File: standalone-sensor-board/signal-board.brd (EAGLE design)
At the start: 26 x 93.5 mm, 32 parts, among them Q1 QRE1113, Q2 QRE1113, Q3 QRE1113, Q4 QRE1113, Q5 QRE1113, Q6 QRE1113, Q7 QRE1113, U1 CD4051BE

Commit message: rough layout
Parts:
- removed FFCIN, FFCOUT: 52806-1410, 52806-1410:528061410
- removed Q1, Q2, Q3, Q4, Q5, Q6, Q7: QRE1113, qre1113:DIP4_100AQ_ONS
- removed R1, R11, R13, R3, R5, R7, R9: 100, rcl:0207/10
- added J1, J3, J4: (no value), 686114148922:686114148922
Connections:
- removed net N$1: Q1.1, R1.2
- removed net N$11: Q6.1, R11.2
- removed net N$13: Q7.1, R13.2
- removed net N$2: FFCOUT.3, R1.1, R11.1, R13.1, R3.1, R5.1, R7.1, R9.1
- removed net N$3: Q2.1, R3.2
- removed net N$5: Q3.1, R5.2
- removed net N$7: Q4.1, R7.2
- net 3V: now also J3.13, J4.13; no longer FFCIN.13, FFCOUT.2
- net A: now also J3.11, J4.11; no longer FFCIN.11, FFCOUT.4
- net B: now also J3.10, J4.10; no longer FFCIN.10, FFCOUT.5
- net C: now also J3.9, J4.9; no longer FFCIN.9, FFCOUT.6
- net C0: now also J1.1; no longer Q1.3
- net C1: now also J1.2; no longer Q2.3
- net C2: now also J1.3; no longer Q3.3
- net C3: now also J1.9; no longer Q4.3
- net C4: now also J1.10; no longer Q5.3
- net C5: now also J1.11; no longer Q6.3
- net C6: now also J1.12; no longer Q7.3
- net DIN: now also J4.8; no longer FFCIN.8
- net DOUT: now also J3.8; no longer FFCOUT.7
- net GND: now also J1.14, J1.MP1, J1.MP2, J3.14, J3.MP1, J3.MP2, J4.14, J4.MP1, J4.MP2; no longer FFCOUT.1, Q1.2, Q1.4, Q2.2, Q2.4, Q3.2, Q3.4, Q4.2, Q4.4, Q5.2, Q5.4, Q6.2, Q6.4, Q7.2, Q7.4
- net S1: now also J3.7, J4.7; no longer FFCIN.7, FFCOUT.8
- net S2: now also J3.6, J4.6; no longer FFCIN.6, FFCOUT.9
- net S3: now also J3.5, J4.5; no longer FFCIN.5, FFCOUT.10
- net S4: now also J3.4, J4.4; no longer FFCIN.4, FFCOUT.11
- net S5: now also J3.3, J4.3; no longer FFCIN.3, FFCOUT.12
- net S6: now also J3.2, J4.2; no longer FFCIN.2, FFCOUT.13
- net S7: now also J3.1, J4.1; no longer FFCIN.1, FFCOUT.14
- net VCC: now also J1.13, J3.12, J4.12; no longer FFCIN.12
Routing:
- net S6: track 89.6 -> 0.00 mm, vias 2 -> 0
- net S4: track 88.9 -> 2.46 mm, vias 2 -> 0
- net S5: track 85.4 -> 3.87 mm, vias 2 -> 0
- net S2: track 85.8 -> 5.08 mm, vias 2 -> 0
- net B: track 79.3 -> 0.00 mm
- net S1: track 79.2 -> 3.02 mm, vias 2 -> 0
- net S3: track 78.6 -> 6.75 mm, vias 2 -> 0
- net C: track 68.1 -> 0.00 mm
- net C1: track 66.8 -> 0.00 mm, vias 3 -> 0
- net A: track 65.9 -> 0.00 mm
- net N$13: track 60.4 -> 0.00 mm
- net C0: track 50.8 -> 0.00 mm
- net N$11: track 49.1 -> 0.00 mm
- net C6: track 48.3 -> 0.00 mm
- net C5: track 29.0 -> 0.00 mm
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
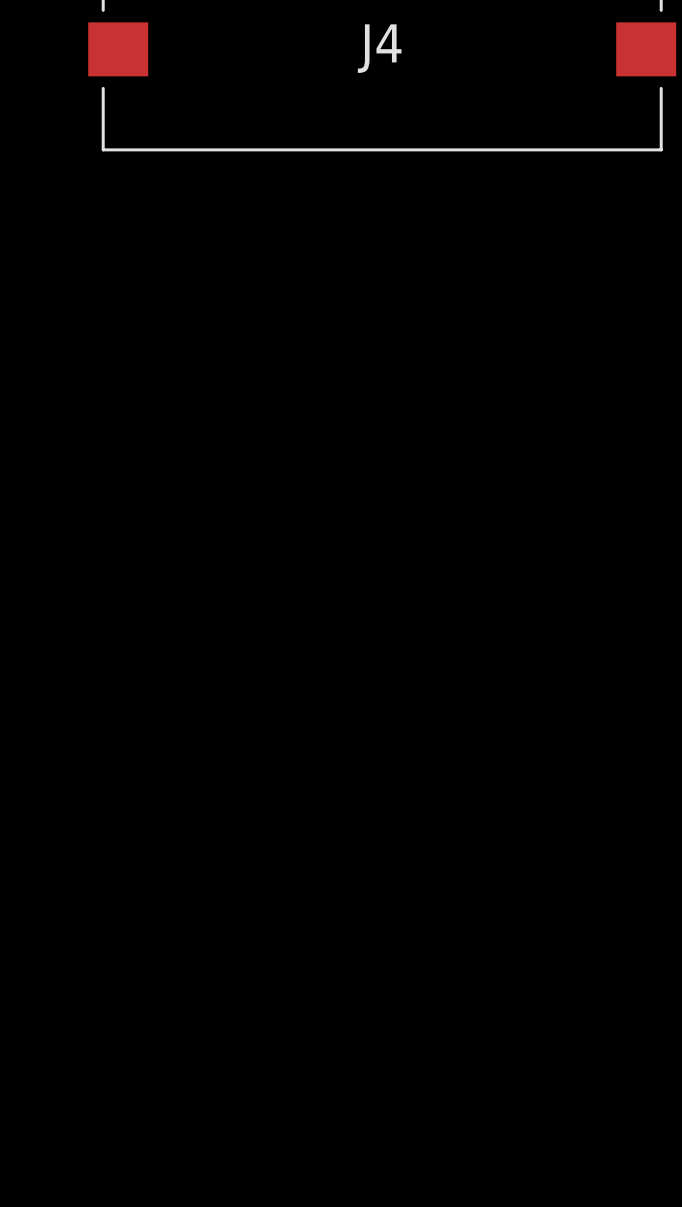
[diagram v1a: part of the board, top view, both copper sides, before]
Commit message: add divider resistors
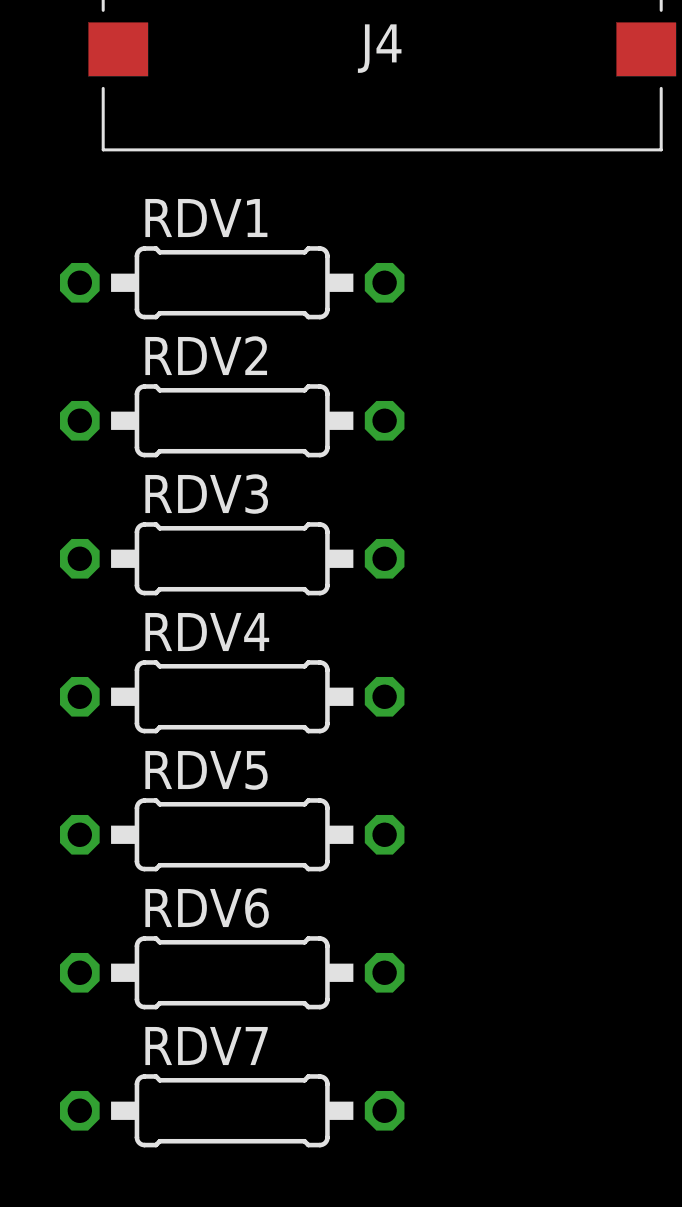
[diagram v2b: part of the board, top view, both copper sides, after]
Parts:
- added RDV1, RDV2, RDV3, RDV4, RDV5, RDV6, RDV7: 100k, rcl:0207/10
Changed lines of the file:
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@@
 <attribute name="VALUE" x="-31.76" y="-40.74" size="1.27" layer="27" align="center"/>
+</element>
+<element name="RDV1" library="rcl" library_urn="urn:adsk.eagle:library:334" package="0207/10" package3d_urn="urn:adsk.eagle:package:23491/2" value="100k" x="-36.76" y="-48.72" smashed="yes">
+<attribute name="NAME" x="-39.808" y="-47.196" size="1.27" layer="25" ratio="10"/>
+<attribute name="POPULARITY" value="81" x="-36.76" y="-48.72" size="1.778" layer="27" display="off"/>
+<attribute name="SPICEPREFIX" value="R" x="-36.76" y="-48.72" size="1.778" layer="27" display="off"/>
+<attribute name="VALUE" x="-39.0206" y="-49.355" size="1.27" layer="27" ratio="10"/>
+</element>
+<element name="RDV2" library="rcl" library_urn="urn:adsk.eagle:library:334" package="0207/10" package3d_urn="urn:adsk.eagle:package:23491/2" value="100k" x="-36.76" y="-53.32" smashed="yes">
+<attribute name="NAME" x="-39.808" y="-51.796" size="1.27" layer="25" ratio="10"/>
+<attribute name="POPULARITY" value="81" x="-36.76" y="-53.32" size="1.778" layer="27" display="off"/>
+<attribute name="SPICEPREFIX" value="R" x="-36.76" y="-53.32" size="1.778" layer="27" display="off"/>
+<attribute name="VALUE" x="-39.0206" y="-53.955" size="1.27" layer="27" ratio="10"/>
+</element>
+<element name="RDV3" library="rcl" library_urn="urn:adsk.eagle:library:334" package="0207/10" package3d_urn="urn:adsk.eagle:package:23491/2" value="100k" x="-36.76" y="-57.92" smashed="yes">
+<attribute name="NAME" x="-39.808" y="-56.396" size="1.27" layer="25" ratio="10"/>
+<attribute name="POPULARITY" value="81" x="-36.76" y="-57.92" size="1.778" layer="27" display="off"/>
+<attribute name="SPICEPREFIX" value="R" x="-36.76" y="-57.92" size="1.778" layer="27" display="off"/>
+<attribute name="VALUE" x="-39.0206" y="-58.555" size="1.27" layer="27" ratio="10"/>
+</element>
+<element name="RDV4" library="rcl" library_urn="urn:adsk.eagle:library:334" package="0207/10" package3d_urn="urn:adsk.eagle:package:23491/2" value="100k" x="-36.76" y="-62.52" smashed="yes">
+<attribute name="NAME" x="-39.808" y="-60.996" size="1.27" layer="25" ratio="10"/>
+<attribute name="POPULARITY" value="81" x="-36.76" y="-62.52" size="1.778" layer="27" display="off"/>
+<attribute name="SPICEPREFIX" value="R" x="-36.76" y="-62.52" size="1.778" layer="27" display="off"/>
+<attribute name="VALUE" x="-39.0206" y="-63.155" size="1.27" layer="27" ratio="10"/>
+</element>
+<element name="RDV5" library="rcl" library_urn="urn:adsk.eagle:library:334" package="0207/10" package3d_urn="urn:adsk.eagle:package:23491/2" value="100k" x="-36.76" y="-67.12" smashed="yes">
+<attribute name="NAME" x="-39.808" y="-65.596" size="1.27" layer="25" ratio="10"/>
+<attribute name="POPULARITY" value="81" x="-36.76" y="-67.12" size="1.778" layer="27" display="off"/>
+<attribute name="SPICEPREFIX" value="R" x="-36.76" y="-67.12" size="1.778" layer="27" display="off"/>
+<attribute name="VALUE" x="-39.0206" y="-67.755" size="1.27" layer="27" ratio="10"/>
+</element>
+<element name="RDV6" library="rcl" library_urn="urn:adsk.eagle:library:334" package="0207/10" package3d_urn="urn:adsk.eagle:package:23491/2" value="100k" x="-36.76" y="-71.72" smashed="yes">
+<attribute name="NAME" x="-39.808" y="-70.196" size="1.27" layer="25" ratio="10"/>
+<attribute name="POPULARITY" value="81" x="-36.76" y="-71.72" size="1.778" layer="27" display="off"/>
+<attribute name="SPICEPREFIX" value="R" x="-36.76" y="-71.72" size="1.778" layer="27" display="off"/>
+<attribute name="VALUE" x="-39.0206" y="-72.355" size="1.27" layer="27" ratio="10"/>
+</element>
+<element name="RDV7" library="rcl" library_urn="urn:adsk.eagle:library:334" package="0207/10" package3d_urn="urn:adsk.eagle:package:23491/2" value="100k" x="-36.76" y="-76.32" smashed="yes">
+<attribute name="NAME" x="-39.808" y="-74.796" size="1.27" layer="25" ratio="10"/>
+<attribute name="POPULARITY" value="81" x="-36.76" y="-76.32" size="1.778" layer="27" display="off"/>
+<attribute name="SPICEPREFIX" value="R" x="-36.76" y="-76.32" size="1.778" layer="27" display="off"/>
+<attribute name="VALUE" x="-39.0206" y="-76.955" size="1.27" layer="27" ratio="10"/>
 </element>
 </elements>

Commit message: set rdvs
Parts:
- removed D1, D2, D3, D4, D5, D6, D7: 1655, 1655:LED_1655
- removed RDV: 100k, rcl:0207/10
- added LED1, LED2, LED3, LED4, LED5, LED6, LED7: WS2812B3535, adafruit:LED3535
- J1: value (none) -> sensors
- J3: value (none) -> to_next_board
- J4: value (none) -> to_controller
- moved J3 128.1 mm to (11.0, 88.7), turned to 180 degrees
- moved RDV7 124.7 mm to (15.1, 37.1)
- moved RDV6 122.9 mm to (15.1, 39.7)
- moved RDV5 121.1 mm to (15.1, 42.3)
- moved RDV4 119.3 mm to (15.1, 44.9)
- moved RDV3 117.5 mm to (15.1, 47.5)
- moved RDV2 115.7 mm to (15.1, 50.1)
- moved RDV1 113.9 mm to (15.1, 52.7)
- moved J1 71.6 mm to (5.00, 47.8), turned to 270 degrees
- moved J4 62.6 mm to (11.1, 4.44)
- moved U1 47.0 mm to (15.4, 14.9), turned to 180 degrees
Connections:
- removed net N$15: D6.4, D7.2
- removed net N$16: D1.4, D2.2
- removed net N$17: D2.4, D3.2
- removed net N$18: D3.4, D4.2
- removed net N$19: D4.4, D5.2
- removed net N$20: D5.4, D6.2
- new net N$1: LED1.3, LED2.1
- new net N$2: LED2.3, LED3.1
- new net N$3: LED3.3, LED4.1
- new net N$4: LED4.3, LED5.1
- new net N$5: LED5.3, LED6.1
- new net N$6: LED6.3, LED7.1
- net 3V: now also LED1.2, LED2.2, LED3.2, LED4.2, LED5.2, LED6.2, LED7.2; no longer D1.3, D2.3, D3.3, D4.3, D5.3, D6.3, D7.3
- net C0: now also RDV1.2
- net C1: now also RDV2.2
- net C2: now also RDV3.2
- net C3: now also RDV4.2
- net C4: now also RDV5.2
- net C5: now also RDV6.2
- net C6: now also RDV7.2
- net DIN: now also LED1.1; no longer D1.2
- net DOUT: now also LED7.3; no longer D7.4
- net GND: now also LED1.4, LED2.4, LED3.4, LED4.4, LED5.4, LED6.4, LED7.4; no longer D1.1, D2.1, D3.1, D4.1, D5.1, D6.1, D7.1
- net SIG: no longer RDV.1
- net VCC: now also RDV1.1, RDV2.1, RDV3.1, RDV4.1, RDV5.1, RDV6.1, RDV7.1; no longer RDV.2
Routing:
- net 3V: track 116.5 -> 0.00 mm
- net GND: track 106.6 -> 0.00 mm, vias 7 -> 0
- net S7: track 79.6 -> 0.00 mm, vias 1 -> 0
- net SIG: track 36.0 -> 0.00 mm
- net VCC: track 19.5 -> 0.00 mm
- net DOUT: track 15.2 -> 0.00 mm, vias 1 -> 0
- net DIN: track 12.9 -> 0.00 mm, vias 1 -> 0
- net N$17: track 12.0 -> 0.00 mm
- net N$20: track 11.3 -> 0.00 mm
- net N$19: track 10.5 -> 0.00 mm
- net N$18: track 10.5 -> 0.00 mm
- net N$15: track 10.4 -> 0.00 mm
- net N$16: track 10.4 -> 0.00 mm
- net S3: track 6.75 -> 0.00 mm
- net S2: track 5.08 -> 0.00 mm
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
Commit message: signal board routing
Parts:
- moved RDV3 25.4 mm to (6.81, 71.5)
- moved U1 24.3 mm to (19.4, 38.9)
- moved RDV2 20.7 mm to (6.81, 69.1)
- moved SJ7 19.4 mm to (3.00, 80.0), flipped to the top, turned to 270 degrees
- moved SJ6 16.6 mm to (5.00, 80.0), flipped to the top, turned to 270 degrees
- moved RDV1 16.3 mm to (6.81, 66.7)
- moved RDV5 14.5 mm to (6.81, 30.4)
- moved RDV6 14.5 mm to (6.81, 27.8)
- moved RDV7 14.5 mm to (6.81, 25.2)
- moved SJ5 13.9 mm to (7.00, 80.0), flipped to the top, turned to 270 degrees
- moved RDV4 13.6 mm to (6.81, 34.0)
- moved SJ4 11.2 mm to (9.00, 80.0), flipped to the top, turned to 270 degrees
- moved SJ3 8.54 mm to (11.0, 80.0), flipped to the top, turned to 270 degrees
- moved SJ2 6.08 mm to (13.0, 80.0), flipped to the top, turned to 270 degrees
- moved SJ1 4.12 mm to (15.0, 80.0), flipped to the top, turned to 270 degrees
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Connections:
- net 3V: now also J3.2; no longer J3.13
- net A: now also J3.4; no longer J3.11
- net B: now also J3.5; no longer J3.10
- net C: now also J3.6; no longer J3.9
- net DOUT: now also J3.7; no longer J3.8
- net GND: now also J3.1; no longer J3.14
- net S1: now also J3.8; no longer J3.7
- net S2: now also J3.9; no longer J3.6
- net S3: now also J3.10; no longer J3.5
- net S4: now also J3.11; no longer J3.4
- net S5: now also J3.12; no longer J3.3
- net S6: now also J3.13; no longer J3.2
- net S7: now also J3.14; no longer J3.1
- net VCC: now also J3.3; no longer J3.12
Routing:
- net VCC: track 0.00 -> 169.6 mm, vias 0 -> 2
- net 3V: track 0.00 -> 160.9 mm, vias 0 -> 9
- net A: track 0.00 -> 91.2 mm, vias 0 -> 2
- net C: track 0.00 -> 90.7 mm, vias 0 -> 2
- net B: track 0.00 -> 90.6 mm, vias 0 -> 2
- net S1: track 0.00 -> 90.4 mm, vias 0 -> 2
- net S2: track 0.00 -> 88.3 mm, vias 0 -> 2
- net S3: track 0.00 -> 86.9 mm, vias 0 -> 2
- net S4: track 0.00 -> 85.5 mm, vias 0 -> 2
- net S5: track 0.00 -> 84.1 mm, vias 0 -> 2
- net S6: track 0.00 -> 83.0 mm, vias 0 -> 2
- net S7: track 0.00 -> 82.9 mm, vias 0 -> 2
- net SIG: track 0.00 -> 51.9 mm
- net C5: track 0.00 -> 47.2 mm
- net C6: track 0.00 -> 41.0 mm
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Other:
- board text added: "NEMUS Signal Board v0.1.0"
- board text removed: "NEMUS Face Board v0.1.1"
